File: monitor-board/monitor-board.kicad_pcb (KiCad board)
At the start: 2 copper layers, 0 parts

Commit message: initial layout of footprints
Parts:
- added D1: LED, LED_SMD:LED_2816_7142Metric_Pad3.20x4.45mm_HandSolder, F.Cu at (44.5, 63.5)
- added J1: Conn_01x06, Connector_PinSocket_2.54mm:PinSocket_1x06_P2.54mm_Vertical, F.Cu at (41.9, 68.6)
- added JBAT1: Conn_01x02, TerminalBlock_Phoenix:TerminalBlock_Phoenix_PT-1,5-2-5.0-H_1x02_P5.00mm_Horizontal, F.Cu at (61.0, 71.1)
- added R1: 10k, Resistor_SMD:R_0805_2012Metric_Pad1.15x1.40mm_HandSolder, F.Cu at (40.6, 50.8)
- added R10: 10k, Resistor_SMD:R_0805_2012Metric_Pad1.15x1.40mm_HandSolder, F.Cu at (66.0, 55.9)
- added R11: 330, Resistor_SMD:R_0805_2012Metric_Pad1.15x1.40mm_HandSolder, F.Cu at (52.1, 63.5)
- added R2: 10k, Resistor_SMD:R_0805_2012Metric_Pad1.15x1.40mm_HandSolder, F.Cu at (40.6, 53.3)
- added R3: 10k, Resistor_SMD:R_0805_2012Metric_Pad1.15x1.40mm_HandSolder, F.Cu at (40.6, 55.9)
- added R4: 10k, Resistor_SMD:R_0805_2012Metric_Pad1.15x1.40mm_HandSolder, F.Cu at (40.6, 58.4)
- added R5: 10k, Resistor_SMD:R_0805_2012Metric_Pad1.15x1.40mm_HandSolder, F.Cu at (66.0, 48.3)
- added R6: 10k, Resistor_SMD:R_0805_2012Metric_Pad1.15x1.40mm_HandSolder, F.Cu at (66.0, 45.7)
- added R7: 10k, Resistor_SMD:R_0805_2012Metric_Pad1.15x1.40mm_HandSolder, F.Cu at (66.0, 43.2)
- added R8: 10k, Resistor_SMD:R_0805_2012Metric_Pad1.15x1.40mm_HandSolder, F.Cu at (66.0, 40.6)
- added R9: 10k, Resistor_SMD:R_0805_2012Metric_Pad1.15x1.40mm_HandSolder, F.Cu at (40.6, 40.6)
- added SW1: SW_IO12, TerminalBlock_Phoenix:TerminalBlock_Phoenix_PT-1,5-2-5.0-H_1x02_P5.00mm_Horizontal, F.Cu at (31.8, 30.6)
- added SW2: SW_IO13, TerminalBlock_Phoenix:TerminalBlock_Phoenix_PT-1,5-2-5.0-H_1x02_P5.00mm_Horizontal, F.Cu at (31.8, 43.2)
- added SW3: SW_IO14, TerminalBlock_Phoenix:TerminalBlock_Phoenix_PT-1,5-2-5.0-H_1x02_P5.00mm_Horizontal, F.Cu at (31.8, 56.0)
- added SW4: SW_IO15, TerminalBlock_Phoenix:TerminalBlock_Phoenix_PT-1,5-2-5.0-H_1x02_P5.00mm_Horizontal, F.Cu at (31.8, 68.6)
- added SW5: SW_IO32, TerminalBlock_Phoenix:TerminalBlock_Phoenix_PT-1,5-2-5.0-H_1x02_P5.00mm_Horizontal, F.Cu at (74.9, 73.6)
- added SW6: SW_IO33, TerminalBlock_Phoenix:TerminalBlock_Phoenix_PT-1,5-2-5.0-H_1x02_P5.00mm_Horizontal, F.Cu at (74.9, 61.0)
- added SW7: SW_IO34, TerminalBlock_Phoenix:TerminalBlock_Phoenix_PT-1,5-2-5.0-H_1x02_P5.00mm_Horizontal, F.Cu at (74.9, 48.3)
- added SW8: SW_IO35, TerminalBlock_Phoenix:TerminalBlock_Phoenix_PT-1,5-2-5.0-H_1x02_P5.00mm_Horizontal, F.Cu at (74.9, 35.6)
- added SW_EN1: SW_EN, TerminalBlock_Phoenix:TerminalBlock_Phoenix_PT-1,5-2-5.0-H_1x02_P5.00mm_Horizontal, F.Cu at (35.6, 83.8)
- added SW_RESET1: SW_RESET, TerminalBlock_Phoenix:TerminalBlock_Phoenix_PT-1,5-2-5.0-H_1x02_P5.00mm_Horizontal, F.Cu at (48.3, 76.2)
- added U1: ESP32-WROOM-32, RF_Module:ESP32-WROOM-32, F.Cu at (53.3, 48.3)
- added U2: TLV75533PDBV, Package_TO_SOT_SMD:SOT-23-5, F.Cu at (61.0, 63.5)
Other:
- rule pad_to_mask_clearance: 0.051 -> 0
- board text removed: "1"
- board text removed: "10/29/2019"
- board text removed: "chris johnston"
- board text removed: "door monitor board 8 output ftdi"

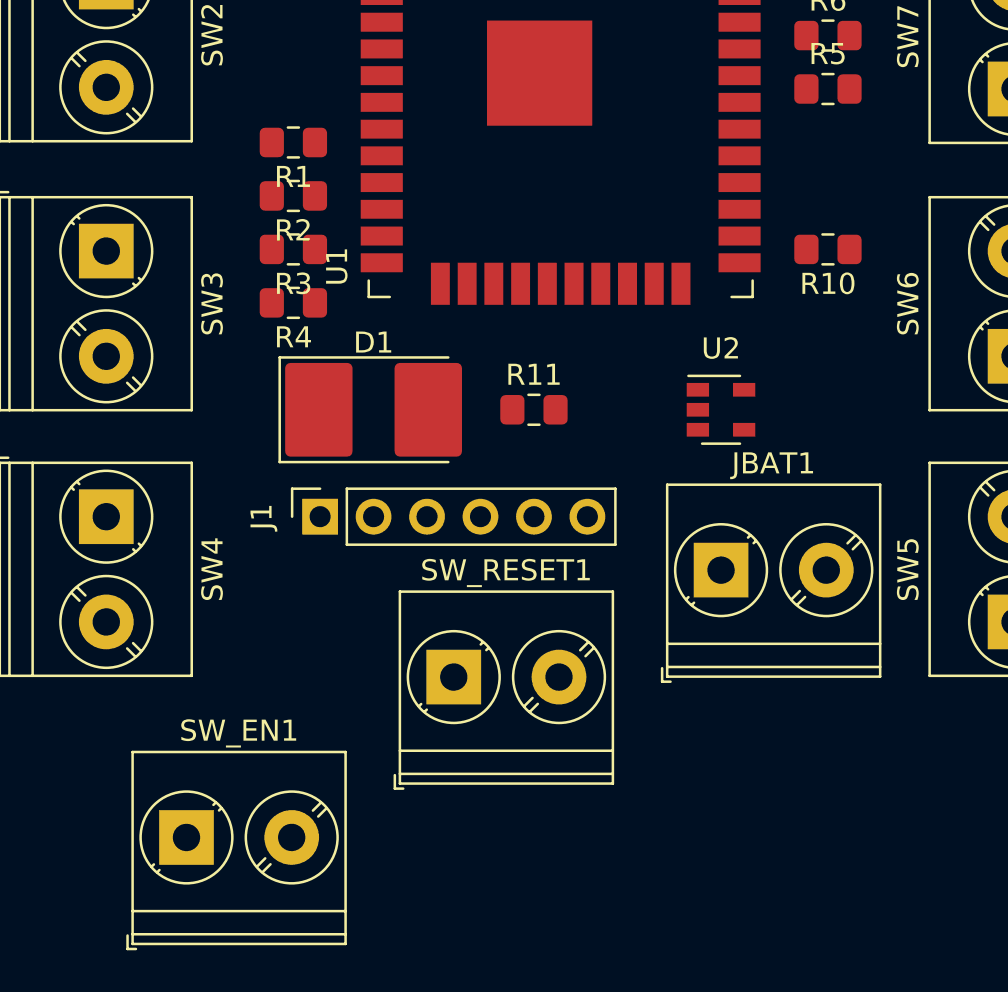
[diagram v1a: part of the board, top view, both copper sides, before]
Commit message: fix footprints of led and switches
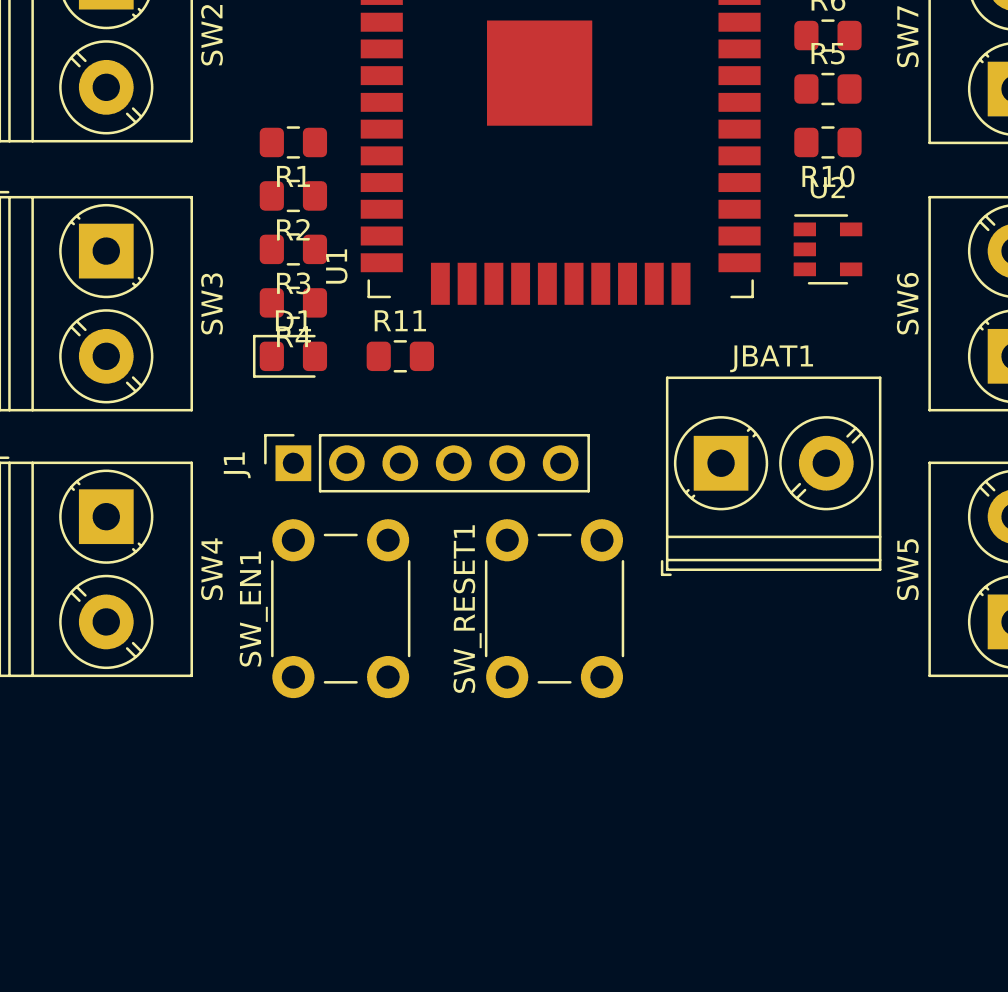
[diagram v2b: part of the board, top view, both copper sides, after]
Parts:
- D1: footprint LED_SMD:LED_2816_7142Metric_Pad3.20x4.45mm_HandSolder -> LED_SMD:LED_0805_2012Metric_Pad1.15x1.40mm_HandSolder
- JBAT1: value Conn_01x02 -> Battery (Max 5.5V DC)
- SW_EN1, SW_RESET1: footprint TerminalBlock_Phoenix:TerminalBlock_Phoenix_PT-1,5-2-5.0-H_1x02_P5.00mm_Horizontal -> Button_Switch_THT:SW_PUSH_6mm
- moved U2 9.16 mm to (66.0, 55.9)
- moved SW_EN1 9.16 mm to (40.6, 76.2), turned to 90 degrees
- moved R11 6.84 mm to (45.7, 61.0)
- moved R10 5.08 mm to (66.0, 50.8)
- moved JBAT1 5.08 mm to (61.0, 66.0)
- moved D1 4.58 mm to (40.6, 61.0)
- moved J1 2.84 mm to (40.6, 66.0)
- moved SW_RESET1 2.54 mm to (50.8, 76.2), turned to 90 degrees

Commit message: add traces
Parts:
- turned R10 to 0 degrees
- turned R9 to 180 degrees
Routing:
- net io_32: track 0.00 -> 54.2 mm, vias 0 -> 2
- net EN: track 0.00 -> 45.0 mm, vias 0 -> 1
- net io_33: track 0.00 -> 44.7 mm, vias 0 -> 2
- net io_35: track 0.00 -> 38.0 mm, vias 0 -> 2
- net io_12: track 0.00 -> 37.3 mm
- net io_34: track 0.00 -> 35.7 mm, vias 0 -> 2
- net io_0: track 0.00 -> 35.1 mm
- net io_15: track 0.00 -> 34.9 mm, vias 0 -> 2
- net io_13: track 0.00 -> 32.6 mm, vias 0 -> 1
- net io_16: track 0.00 -> 20.1 mm
- net io_14: track 0.00 -> 20.0 mm, vias 0 -> 2
- net +BATT: track 0.00 -> 14.3 mm
- net +3V3: track 0.00 -> 3.44 mm
- net Net-(D1-Pad2): track 0.00 -> 3.03 mm
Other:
- net class Default: clearance 0.2 -> 0.1
- rule trace_clearance: 0.2 -> 0.1

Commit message: finish routing the PCB
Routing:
- net +3V3: track 3.44 -> 58.5 mm, vias 0 -> 5
- net -BATT: track 0.00 -> 44.5 mm, vias 0 -> 3
- net RX_FTDI: track 0.00 -> 30.9 mm, vias 0 -> 2
- net TX_FTDI: track 0.00 -> 29.7 mm, vias 0 -> 2
- net io_13: vias 1 -> 0
- added copper zone on B.Cu, net -BATT
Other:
- board outline added: 55.9 x 53.3 mm
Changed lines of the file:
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@@
   (general
     (thickness 1.6)
-    (drawings 0)
-    (tracks 146)
+    (drawings 4)
+    (tracks 213)
     (zones 0)
     (modules 26)
@@
     )
   )
+  (gr_line (start 81.28 25.4) (end 25.4 25.4) (layer Edge.Cuts) (width 0.15))
+  (gr_line (start 81.28 78.74) (end 81.28 25.4) (layer Edge.Cuts) (width 0.15))
+  (gr_line (start 25.4 78.74) (end 81.28 78.74) (layer Edge.Cuts) (width 0.15))
+  (gr_line (start 25.4 25.4) (end 25.4 78.74) (layer Edge.Cuts) (width 0.15))
+  (via (at 52.324 51.308) (size 0.8) (drill 0.4) (layers F.Cu B.Cu) (net 1))
+  (segment (start 52.34 47.505) (end 52.34 51.292) (width 0.25) (layer F.Cu) (net 1))
+  (segment (start 52.34 51.292) (end 52.324 51.308) (width 0.25) (layer F.Cu) (net 1))
+  (segment (start 47.625 56.007) (end 47.625 57.515) (width 0.25) (layer F.Cu) (net 1))
+  (segment (start 52.324 51.308) (end 47.625 56.007) (width 0.25) (layer F.Cu) (net 1))
+  (via (at 40.64 59.944) (size 0.8) (drill 0.4) (layers F.Cu B.Cu) (net 1))
+  (segment (start 39.615 60.96) (end 39.624 60.96) (width 0.25) (layer F.Cu) (net 1))
+  (segment (start 39.624 60.96) (end 40.64 59.944) (width 0.25) (layer F.Cu) (net 1))
+  (segment (start 44.84 40.005) (end 61.84 40.005) (width 0.25) (layer F.Cu) (net 1))
+  (segment (start 52.34 44.755) (end 52.34 47.505) (width 0.25) (layer F.Cu) (net 1))
+  (segment (start 47.59 40.005) (end 52.34 44.755) (width 0.25) (layer F.Cu) (net 1))
+  (segment (start 44.84 40.005) (end 47.59 40.005) (width 0.25) (layer F.Cu) (net 1))
+  (via (at 63.5 56.896) (size 0.8) (drill 0.4) (layers F.Cu B.Cu) (net 1))
+  (segment (start 64.94 55.88) (end 64.516 55.88) (width 0.25) (layer F.Cu) (net 1))
+  (segment (start 64.516 55.88) (end 63.5 56.896) (width 0.25) (layer F.Cu) (net 1))
   (segment (start 41.665 60.96) (end 44.695 60.96) (width 0.25) (layer F.Cu) (net 2))
+  (via (at 48.26 62.992) (size 0.8) (drill 0.4) (layers F.Cu B.Cu) (net 5))
+  (segment (start 48.26 66.04) (end 48.26 62.992) (width 0.25) (layer F.Cu) (net 5))
+  (segment (start 48.26 62.992) (end 50.8 62.992) (width 0.25) (layer B.Cu) (net 5))
+  (segment (start 50.8 62.992) (end 58.928 54.864) (width 0.25) (layer B.Cu) (net 5))
+  (via (at 58.928 50.8) (size 0.8) (drill 0.4) (layers F.Cu B.Cu) (net 5))
+  (segment (start 58.928 54.864) (end 58.928 50.8) (width 0.25) (layer B.Cu) (net 5))
+  (segment (start 58.928 50.8) (end 58.928 45.212) (width 0.25) (layer F.Cu) (net 5))
+  (segment (start 59.055 45.085) (end 61.84 45.085) (width 0.25) (layer F.Cu) (net 5))
+  (segment (start 58.928 45.212) (end 59.055 45.085) (width 0.25) (layer F.Cu) (net 5))
+  (via (at 50.8 64.008) (size 0.8) (drill 0.4) (layers F.Cu B.Cu) (net 6))
+  (segment (start 50.8 66.04) (end 50.8 64.008) (width 0.25) (layer F.Cu) (net 6))
+  (segment (start 51.199999 63.608001) (end 51.199999 63.100001) (width 0.25) (layer B.Cu) (net 6))
+  (segment (start 50.8 64.008) (end 51.199999 63.608001) (width 0.25) (layer B.Cu) (net 6))
+  (segment (start 58.928 55.372) (end 58.928 55.358988) (width 0.25) (layer B.Cu) (net 6))
+  (segment (start 51.199999 63.100001) (end 58.928 55.372) (width 0.25) (layer B.Cu) (net 6))
+  (via (at 59.944 51.308) (size 0.8) (drill 0.4) (layers F.Cu B.Cu) (net 6))
+  (segment (start 58.928 55.358988) (end 59.944 54.342988) (width 0.25) (layer B.Cu) (net 6))
+  (segment (start 59.944 54.342988) (end 59.944 51.308) (width 0.25) (layer B.Cu) (net 6))
+  (segment (start 59.944 51.308) (end 59.436 51.816) (width 0.25) (layer F.Cu) (net 6))
+  (segment (start 58.302999 51.100001) (end 58.302999 44.821001) (width 0.25) (layer F.Cu) (net 6))
+  (segment (start 59.436 51.816) (end 59.018998 51.816) (width 0.25) (layer F.Cu) (net 6))
+  (segment (start 59.018998 51.816) (end 58.302999 51.100001) (width 0.25) (layer F.Cu) (net 6))
+  (segment (start 59.309 43.815) (end 61.84 43.815) (width 0.25) (layer F.Cu) (net 6))
+  (segment (start 58.302999 44.821001) (end 59.309 43.815) (width 0.25) (layer F.Cu) (net 6))
   (segment (start 65.250002 54.93) (end 66.04 55.719998) (width 0.25) (layer F.Cu) (net 8))
   (segment (start 64.94 54.93) (end 65.250002 54.93) (width 0.25) (layer F.Cu) (net 8))
@@
   (segment (start 42.3 41.275) (end 44.84 41.275) (width 0.25) (layer F.Cu) (net 9))
   (segment (start 41.665 40.64) (end 42.3 41.275) (width 0.25) (layer F.Cu) (net 9))
+  (segment (start 65.015 40.64) (end 65.015 43.18) (width 0.25) (layer F.Cu) (net 9))
+  (segment (start 65.015 43.18) (end 65.015 45.72) (width 0.25) (layer F.Cu) (net 9))
+  (segment (start 65.015 45.72) (end 65.015 48.26) (width 0.25) (layer F.Cu) (net 9))
+  (segment (start 65.015 48.26) (end 65.015 50.8) (width 0.25) (layer F.Cu) (net 9))
+  (segment (start 41.665 58.42) (end 41.665 55.88) (width 0.25) (layer F.Cu) (net 9))
+  (segment (start 41.665 55.88) (end 41.665 53.34) (width 0.25) (layer F.Cu) (net 9))
+  (via (at 43.18 58.928) (size 0.8) (drill 0.4) (layers F.Cu B.Cu) (net 9))
+  (segment (start 41.665 58.42) (end 42.672 58.42) (width 0.25) (layer F.Cu) (net 9))
+  (segment (start 42.672 58.42) (end 43.18 58.928) (width 0.25) (layer F.Cu) (net 9))
+  (segment (start 43.18 58.928) (end 42.672 58.42) (width 0.25) (layer B.Cu) (net 9))
+  (segment (start 40.984998 58.42) (end 39.116 56.551002) (width 0.25) (layer B.Cu) (net 9))
+  (segment (start 42.672 58.42) (end 40.984998 58.42) (width 0.25) (layer B.Cu) (net 9))
+  (segment (start 39.116 56.551002) (end 39.116 52.324) (width 0.25) (layer B.Cu) (net 9))
+  (via (at 41.665 50.8) (size 0.8) (drill 0.4) (layers F.Cu B.Cu) (net 9))
+  (segment (start 39.116 52.324) (end 40.64 50.8) (width 0.25) (layer B.Cu) (net 9))
+  (segment (start 40.64 50.8) (end 41.665 50.8) (width 0.25) (layer B.Cu) (net 9))
+  (segment (start 39.116 52.324) (end 39.116 39.116) (width 0.25) (layer B.Cu) (net 9))
+  (segment (start 39.116 39.116) (end 41.656 39.116) (width 0.25) (layer B.Cu) (net 9))
+  (via (at 41.656 39.116) (size 0.8) (drill 0.4) (layers F.Cu B.Cu) (net 9))
+  (segment (start 41.656 40.631) (end 41.665 40.64) (width 0.25) (layer F.Cu) (net 9))
+  (segment (start 41.656 39.116) (end 41.656 40.631) (width 0.25) (layer F.Cu) (net 9))
+  (via (at 63.5 50.8) (size 0.8) (drill 0.4) (layers F.Cu B.Cu) (net 9))
+  (segment (start 65.015 50.8) (end 63.5 50.8) (width 0.25) (layer F.Cu) (net 9))
+  (segment (start 63.5 50.8) (end 63.5 51.816) (width 0.25) (layer B.Cu) (net 9))
+  (segment (start 63.5 51.816) (end 65.024 53.34) (width 0.25) (layer B.Cu) (net 9))
+  (segment (start 65.024 53.34) (end 67.056 53.34) (width 0.25) (layer B.Cu) (net 9))
+  (via (at 67.056 53.34) (size 0.8) (drill 0.4) (layers F.Cu B.Cu) (net 9))
+  (segment (start 67.056 54.846) (end 67.14 54.93) (width 0.25) (layer F.Cu) (net 9))
+  (segment (start 67.056 53.34) (end 67.056 54.846) (width 0.25) (layer F.Cu) (net 9))
   (segment (start 38.991628 50.176628) (end 39.615 50.8) (width 0.25) (layer F.Cu) (net 10))
   (segment (start 37.474999 48.659999) (end 38.991628 50.176628) (width 0.25) (layer F.Cu) (net 10))
@@
   (segment (start 35.56 49.285) (end 39.615 53.34) (width 0.25) (layer F.Cu) (net 11))
   (segment (start 35.56 43.18) (end 35.56 49.285) (width 0.25) (layer F.Cu) (net 11))
-  (via (at 39.615 53.34) (size 0.8) (drill 0.4) (layers F.Cu B.Cu) (net 11))
   (segment (start 48.895 58.065) (end 48.895 57.515) (width 0.25) (layer F.Cu) (net 11))
   (segment (start 47.905 59.055) (end 48.895 58.065) (width 0.25) (layer F.Cu) (net 11))
@@
   (segment (start 57.925012 60.96) (end 60.325 58.560012) (width 0.25) (layer F.Cu) (net 20))
   (segment (start 46.745 60.96) (end 57.925012 60.96) (width 0.25) (layer F.Cu) (net 20))
+  (zone (net 1) (net_name -BATT) (layer B.Cu) (hatch edge 0.508)
+    (connect_pads (clearance 0.508))
+    (min_thickness 0.254)
+    (fill yes (arc_segments 32) (thermal_gap 0.508) (thermal_bridge_width 0.508))
+    (polygon
+      (pts
+        (xy 25.908 25.908) (xy 80.772 25.908) (xy 80.772 78.232) (xy 25.908 78.232)
+      )
+    )
+  )
 )

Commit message: leave a TODO
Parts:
- renumbered J1 to FTDI
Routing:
- net +3V3: track 58.5 -> 80.8 mm, vias 5 -> 7
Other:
- board text added: "+ - MAX: 5.5VDC"
- board text added: "3.3VDC ONLY!"
- board text added: "Chris Johnston 10/30/2019 github.com/Chris-Johnston"
- board text added: "GND"
- board text added: "RX"
- board text added: "TX"
- board text added: "Warranty void if sticker removed"
- board text added: "hey you have to put the board together first"
- board text added: "todo check the U1 power regulartor footprint, I don't think that it is right"
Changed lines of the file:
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@@
   (general
     (thickness 1.6)
-    (drawings 4)
-    (tracks 213)
+    (drawings 13)
+    (tracks 224)
     (zones 0)
     (modules 26)
@@
     (descr "Through hole straight socket strip, 1x06, 2.54mm pitch, single row (from Kicad 4.0.7), script generated")
     (tags "Through hole socket strip THT 1x06 2.54mm single row")
-    (fp_text reference J1 (at 0 -2.77 90) (layer F.SilkS)
+    (fp_text reference FTDI (at 0 -2.77 90) (layer F.SilkS)
       (effects (font (size 1 1) (thickness 0.15)))
     )
@@
       (rotate (xyz 0 0 0))
     )
+  )
+  (gr_text "todo check the U1 power regulartor footprint, I don't think that it is right\n" (at 73.66 20.32) (layer F.Cu)
+    (effects (font (size 1.5 1.5) (thickness 0.3)))
+  )
+  (gr_text "3.3VDC ONLY!" (at 51.816 61.976) (layer F.SilkS)
+    (effects (font (size 0.7 0.7) (thickness 0.15)))
+  )
+  (gr_text RX (at 50.8 64.008 90) (layer F.SilkS)
+    (effects (font (size 0.5 0.5) (thickness 0.125)))
+  )
+  (gr_text TX (at 48.26 64.008 90) (layer F.SilkS)
+    (effects (font (size 0.5 0.5) (thickness 0.125)))
+  )
+  (gr_text GND (at 40.64 64.008 90) (layer F.SilkS)
+    (effects (font (size 0.5 0.5) (thickness 0.125)))
+  )
+  (gr_text "Chris Johnston 10/30/2019\ngithub.com/Chris-Johnston" (at 48.26 28.448) (layer F.SilkS)
+    (effects (font (size 1 1) (thickness 0.15)))
+  )
+  (gr_text "hey you have\nto put the board\ntogether first" (at 52.832 52.324) (layer F.SilkS)
+    (effects (font (size 1 1) (thickness 0.15)))
+  )
+  (gr_text "Warranty void if sticker removed" (at 66.548 77.216) (layer F.SilkS)
+    (effects (font (size 1 0.7) (thickness 0.1)))
+  )
+  (gr_text "+     -\nMAX: 5.5VDC" (at 62.992 73.152) (layer F.SilkS)
+    (effects (font (size 1 1) (thickness 0.15)))
   )
   (gr_line (start 81.28 25.4) (end 25.4 25.4) (layer Edge.Cuts) (width 0.15))
@@
   (segment (start 67.056 54.846) (end 67.14 54.93) (width 0.25) (layer F.Cu) (net 9))
   (segment (start 67.056 53.34) (end 67.056 54.846) (width 0.25) (layer F.Cu) (net 9))
+  (segment (start 46.09 41.275) (end 46.217 41.148) (width 0.25) (layer F.Cu) (net 9))
+  (segment (start 44.84 41.275) (end 46.09 41.275) (width 0.25) (layer F.Cu) (net 9))
+  (via (at 47.752 41.148) (size 0.8) (drill 0.4) (layers F.Cu B.Cu) (net 9))
+  (segment (start 46.217 41.148) (end 47.752 41.148) (width 0.25) (layer F.Cu) (net 9))
+  (segment (start 47.752 41.148) (end 55.372 41.148) (width 0.25) (layer B.Cu) (net 9))
+  (segment (start 55.372 41.148) (end 57.404 39.116) (width 0.25) (layer B.Cu) (net 9))
+  (via (at 64.008 39.116) (size 0.8) (drill 0.4) (layers F.Cu B.Cu) (net 9))
+  (segment (start 57.404 39.116) (end 64.008 39.116) (width 0.25) (layer B.Cu) (net 9))
+  (segment (start 64.008 39.116) (end 64.516 39.116) (width 0.25) (layer F.Cu) (net 9))
+  (segment (start 65.015 39.615) (end 65.015 40.64) (width 0.25) (layer F.Cu) (net 9))
+  (segment (start 64.516 39.116) (end 65.015 39.615) (width 0.25) (layer F.Cu) (net 9))
   (segment (start 38.991628 50.176628) (end 39.615 50.8) (width 0.25) (layer F.Cu) (net 10))
   (segment (start 37.474999 48.659999) (end 38.991628 50.176628) (width 0.25) (layer F.Cu) (net 10))

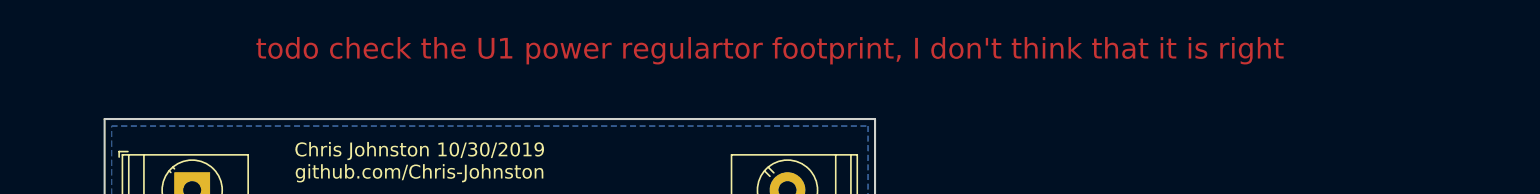
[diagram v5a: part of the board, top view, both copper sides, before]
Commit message: remove todo text, part matched footprint
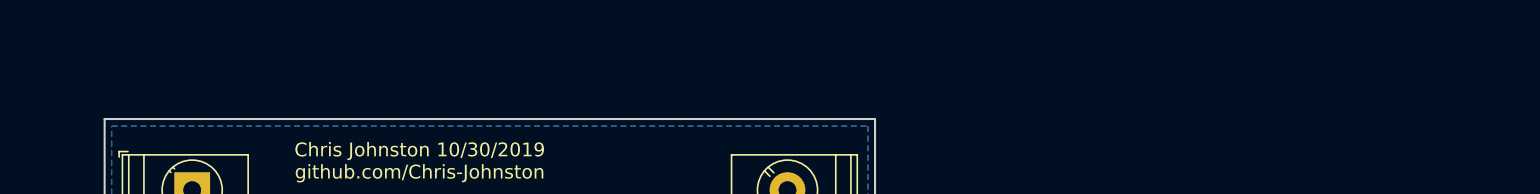
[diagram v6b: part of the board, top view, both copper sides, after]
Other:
- board text removed: "todo check the U1 power regulartor footprint, I don't think that it is right"
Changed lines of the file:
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@@
   (general
     (thickness 1.6)
-    (drawings 13)
+    (drawings 12)
     (tracks 224)
     (zones 0)
@@
     )
   )
-  (gr_text "todo check the U1 power regulartor footprint, I don't think that it is right\n" (at 73.66 20.32) (layer F.Cu)
-    (effects (font (size 1.5 1.5) (thickness 0.3)))
-  )
   (gr_text "3.3VDC ONLY!" (at 51.816 61.976) (layer F.SilkS)
